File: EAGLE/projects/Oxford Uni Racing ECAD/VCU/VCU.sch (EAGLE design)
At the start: 25 parts, among them J1 PWR_CAN, J2 ASS, J3 MC_LEFT, J4 MC_RIGHT, K1 RT444012, X2 D-SUB9-H2M09ST

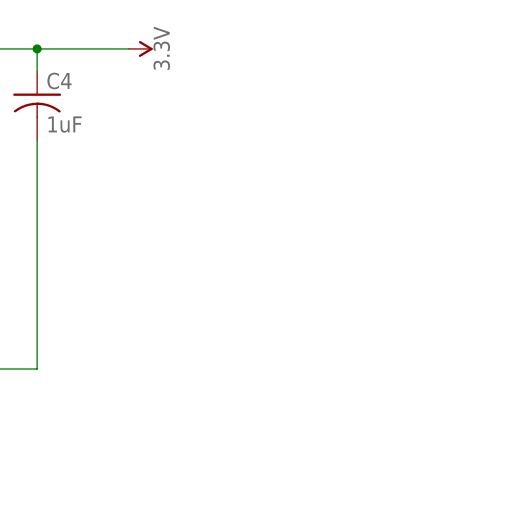
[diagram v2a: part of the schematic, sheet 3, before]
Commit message: added indicator LEDs to boards
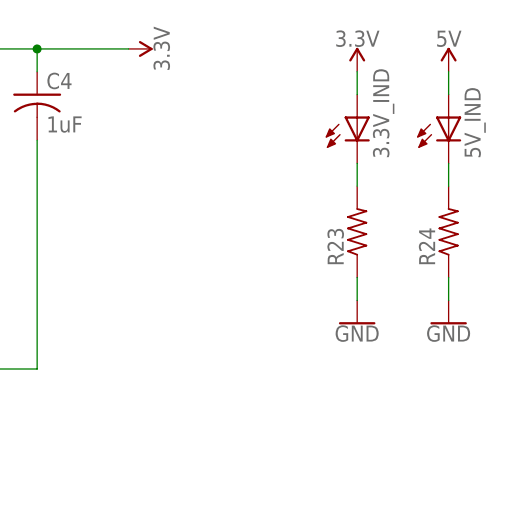
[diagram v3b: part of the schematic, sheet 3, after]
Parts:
- added 3.3V_IND, 5V_IND: (no value), adafruit:LED3MM
- added R23, R24: (no value), adafruit:R-US_0204/7
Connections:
- new net N$12: 3.3V_IND.C, R23.2
- new net N$5: 5V_IND.C, R24.2
- net 3.3V: now also 3.3V_IND.A
- net 5V: now also 5V_IND.A
- net GND: now also R23.1, R24.1
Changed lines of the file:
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@@
 <part name="J2" library="T821108A1S100CEU" deviceset="T821108A1S100CEU" device="" value="ASS"/>
 <part name="F1" library="fuse" library_urn="urn:adsk.eagle:library:233" deviceset="FUSE" device="BLANK_5X20MM" package3d_urn="urn:adsk.eagle:package:14079/1" value="1A"/>
+<part name="3.3V_IND" library="adafruit" library_urn="urn:adsk.eagle:library:420" deviceset="LED" device="3MM" package3d_urn="urn:adsk.eagle:package:6240537/1"/>
+<part name="R23" library="adafruit" library_urn="urn:adsk.eagle:library:420" deviceset="R-US_" device="0204/7" package3d_urn="urn:adsk.eagle:package:6240596/1"/>
+<part name="SUPPLY47" library="SparkFun-PowerSymbols" library_urn="urn:adsk.eagle:library:530" deviceset="3.3V" device=""/>
+<part name="GND30" library="SparkFun-PowerSymbols" library_urn="urn:adsk.eagle:library:530" deviceset="GND" device=""/>
+<part name="5V_IND" library="adafruit" library_urn="urn:adsk.eagle:library:420" deviceset="LED" device="3MM" package3d_urn="urn:adsk.eagle:package:6240537/1"/>
+<part name="R24" library="adafruit" library_urn="urn:adsk.eagle:library:420" deviceset="R-US_" device="0204/7" package3d_urn="urn:adsk.eagle:package:6240596/1"/>
+<part name="SUPPLY54" library="SparkFun-PowerSymbols" library_urn="urn:adsk.eagle:library:530" deviceset="5V" device=""/>
+<part name="GND33" library="SparkFun-PowerSymbols" library_urn="urn:adsk.eagle:library:530" deviceset="GND" device=""/>
 </parts>
 <sheets>
@@
 <attribute name="VALUE" x="114.3" y="9.906" size="1.778" layer="96" align="top-center"/>
 </instance>
+<instance part="3.3V_IND" gate="G$1" x="170.18" y="96.52" smashed="yes">
+<attribute name="NAME" x="173.736" y="91.948" size="1.778" layer="95" rot="R90"/>
+<attribute name="VALUE" x="175.895" y="91.948" size="1.778" layer="96" rot="R90"/>
+</instance>
+<instance part="R23" gate="G$1" x="170.18" y="83.82" smashed="yes" rot="R90">
+<attribute name="NAME" x="168.6814" y="80.01" size="1.778" layer="95" rot="R90"/>
+<attribute name="VALUE" x="173.482" y="80.01" size="1.778" layer="96" rot="R90"/>
+</instance>
+<instance part="SUPPLY47" gate="G$1" x="170.18" y="101.6" smashed="yes">
+<attribute name="VALUE" x="170.18" y="104.394" size="1.778" layer="96" align="bottom-center"/>
+</instance>
+<instance part="GND30" gate="1" x="170.18" y="73.66" smashed="yes">
+<attribute name="VALUE" x="170.18" y="73.406" size="1.778" layer="96" align="top-center"/>
+</instance>
+<instance part="5V_IND" gate="G$1" x="180.34" y="96.52" smashed="yes">
+<attribute name="NAME" x="183.896" y="91.948" size="1.778" layer="95" rot="R90"/>
+<attribute name="VALUE" x="186.055" y="91.948" size="1.778" layer="96" rot="R90"/>
+</instance>
+<instance part="R24" gate="G$1" x="180.34" y="83.82" smashed="yes" rot="R90">
+<attribute name="NAME" x="178.8414" y="80.01" size="1.778" layer="95" rot="R90"/>
+<attribute name="VALUE" x="183.642" y="80.01" size="1.778" layer="96" rot="R90"/>
+</instance>
+<instance part="SUPPLY54" gate="G$1" x="180.34" y="101.6" smashed="yes">
+<attribute name="VALUE" x="180.34" y="104.394" size="1.778" layer="96" align="bottom-center"/>
+</instance>
+<instance part="GND33" gate="1" x="180.34" y="73.66" smashed="yes">
+<attribute name="VALUE" x="180.34" y="73.406" size="1.778" layer="96" align="top-center"/>
+</instance>
 </instances>
 <busses>
@@
 <junction x="124.46" y="48.26"/>
 </segment>
+<segment>
+<pinref part="5V_IND" gate="G$1" pin="A"/>
+<pinref part="SUPPLY54" gate="G$1" pin="5V"/>
+<wire x1="180.34" y1="99.06" x2="180.34" y2="101.6" width="0.1524" layer="91"/>
+</segment>
 </net>
 <net name="3.3V" class="0">
@@
 <pinref part="SUPPLY25" gate="G$1" pin="3.3V"/>
 </segment>
+<segment>
+<pinref part="3.3V_IND" gate="G$1" pin="A"/>
+<pinref part="SUPPLY47" gate="G$1" pin="3.3V"/>
+<wire x1="170.18" y1="99.06" x2="170.18" y2="101.6" width="0.1524" layer="91"/>
+</segment>
 </net>
 <net name="GND" class="0">
@@
 <wire x1="134.62" y1="12.7" x2="114.3" y2="12.7" width="0.1524" layer="91"/>
 </segment>
+<segment>
+<pinref part="R24" gate="G$1" pin="1"/>
+<pinref part="GND33" gate="1" pin="GND"/>
+<wire x1="180.34" y1="78.74" x2="180.34" y2="76.2" width="0.1524" layer="91"/>
+</segment>
+<segment>
+<pinref part="GND30" gate="1" pin="GND"/>
+<pinref part="R23" gate="G$1" pin="1"/>
+<wire x1="170.18" y1="76.2" x2="170.18" y2="78.74" width="0.1524" layer="91"/>
+</segment>
 </net>
 <net name="CANH" class="0">
@@
 </segment>
 </net>
+<net name="N$5" class="0">
+<segment>
+<pinref part="5V_IND" gate="G$1" pin="C"/>
+<pinref part="R24" gate="G$1" pin="2"/>
+<wire x1="180.34" y1="91.44" x2="180.34" y2="88.9" width="0.1524" layer="91"/>
+</segment>
+</net>
+<net name="N$12" class="0">
+<segment>
+<pinref part="R23" gate="G$1" pin="2"/>
+<pinref part="3.3V_IND" gate="G$1" pin="C"/>
+<wire x1="170.18" y1="88.9" x2="170.18" y2="91.44" width="0.1524" layer="91"/>
+</segment>
+</net>

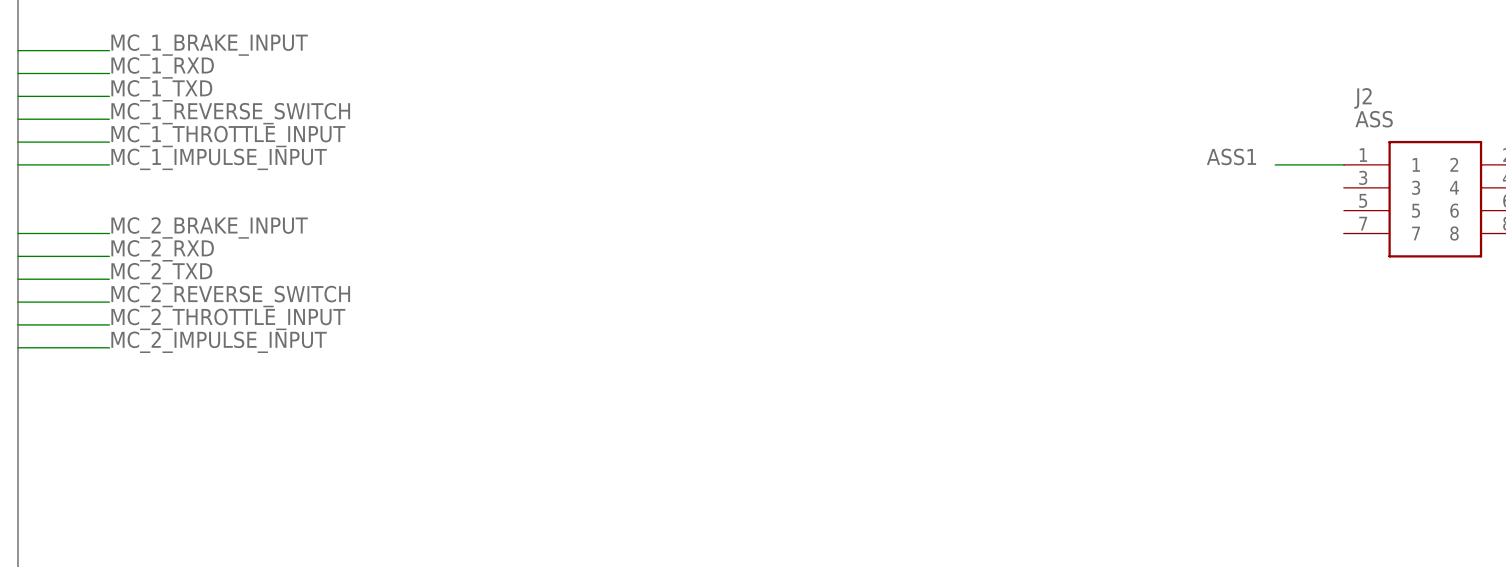
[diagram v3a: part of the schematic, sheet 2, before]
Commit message: added air coil connection on VCU
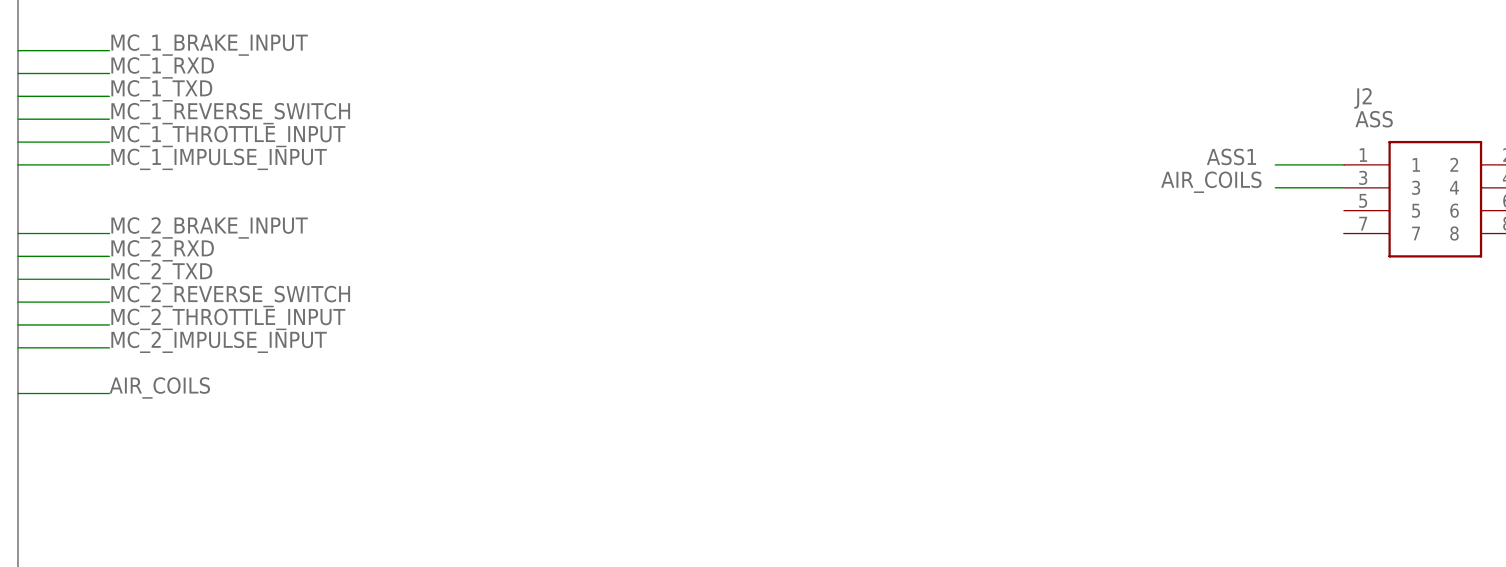
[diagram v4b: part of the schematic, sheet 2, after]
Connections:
- new net AIR_COILS: J2.3, U$1.J5030-D7
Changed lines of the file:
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@@
+</segment>
+</net>
+<net name="AIR_COILS" class="0">
+<segment>
+<wire x1="0" y1="27.94" x2="10.16" y2="27.94" width="0.1524" layer="91"/>
+<label x="10.16" y="27.94" size="1.778" layer="95"/>
 </segment>
 </net>
@@
 </segment>
 </net>
+<net name="AIR_COILS" class="0">
+<segment>
+<wire x1="0" y1="27.94" x2="10.16" y2="27.94" width="0.1524" layer="91"/>
+<label x="10.16" y="27.94" size="1.778" layer="95"/>
+</segment>
+<segment>
+<pinref part="J2" gate="G$1" pin="3"/>
+<wire x1="147.32" y1="50.8" x2="139.7" y2="50.8" width="0.1524" layer="91"/>
+<label x="127" y="50.8" size="1.778" layer="95"/>
+</segment>
+</net>
 </nets>
 </sheet>
@@
 </segment>
 </net>
+<net name="AIR_COILS" class="0">
+<segment>
+<wire x1="0" y1="27.94" x2="10.16" y2="27.94" width="0.1524" layer="91"/>
+<label x="10.16" y="27.94" size="1.778" layer="95"/>
+</segment>
+</net>
 </nets>
 </sheet>
@@
 </instances>
 <busses>
-<bus name="3.3V,5V,12V,ASS1,ASS2,CANH,CANL,GND,MC_1_BRAKE_INPUT,MC_1_IMPULSE_INPUT,MC_1_REVERSE_SWITCH,MC_1_RXD,MC_1_THROTTLE_INPUT,MC_1_TXD,MC_2_BRAKE_INPUT,MC_2_IMPULSE_INPUT,MC_2_REVERSE_SWITCH,MC_2_RXD,MC_2_THROTTLE_INPUT,MC_2_TXD">
+<bus name="3.3V,5V,12V,AIR_COILS,ASS1,ASS2,CANH,CANL,GND,MC_1_BRAKE_INPUT,MC_1_IMPULSE_INPUT,MC_1_REVERSE_SWITCH,MC_1_RXD,MC_1_THROTTLE_INPUT,MC_1_TXD,MC_2_BRAKE_INPUT,MC_2_IMPULSE_INPUT,MC_2_REVERSE_SWITCH,MC_2_RXD,MC_2_THROTTLE_INPUT,MC_2_TXD">
 <segment>
 <wire x1="0" y1="0" x2="0" y2="96.52" width="0.762" layer="92"/>
@@
 <pinref part="BR_LIGHTS_TR" gate="G$1" pin="D"/>
 <wire x1="360.68" y1="132.08" x2="360.68" y2="121.92" width="0.1524" layer="91"/>
+</segment>
+</net>
+<net name="AIR_COILS" class="0">
+<segment>
+<pinref part="U$1" gate="G$1" pin="J5030-D7"/>
+<wire x1="287.02" y1="83.82" x2="304.8" y2="83.82" width="0.1524" layer="91"/>
+<label x="304.8" y="83.82" size="1.778" layer="95"/>
+</segment>
+<segment>
+<wire x1="0" y1="27.94" x2="10.16" y2="27.94" width="0.1524" layer="91"/>
+<label x="10.16" y="27.94" size="1.778" layer="95"/>
 </segment>
 </net>
@@
 </segment>
 </net>
+<net name="AIR_COILS" class="0">
+<segment>
+<wire x1="0" y1="27.94" x2="10.16" y2="27.94" width="0.1524" layer="91"/>
+<label x="10.16" y="27.94" size="1.778" layer="95"/>
+</segment>
+</net>
 </nets>
 </sheet>
@@
 </segment>
 </net>
+<net name="AIR_COILS" class="0">
+<segment>
+<wire x1="0" y1="27.94" x2="10.16" y2="27.94" width="0.1524" layer="91"/>
+<label x="10.16" y="27.94" size="1.778" layer="95"/>
+</segment>
+</net>

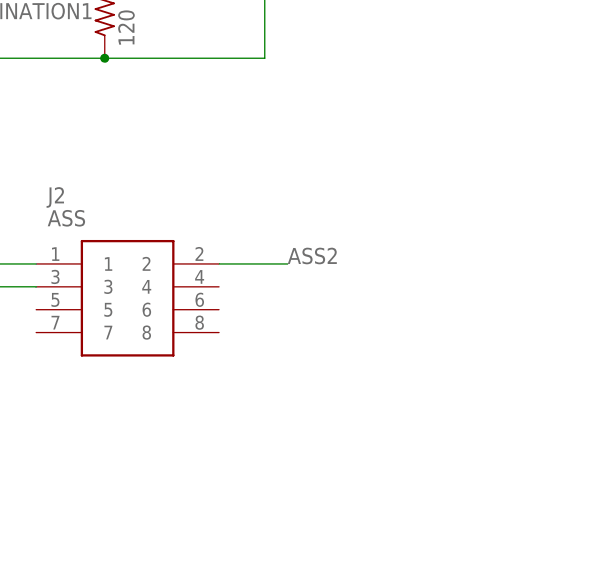
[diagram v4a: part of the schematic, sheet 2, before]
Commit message: added power pin for air coils
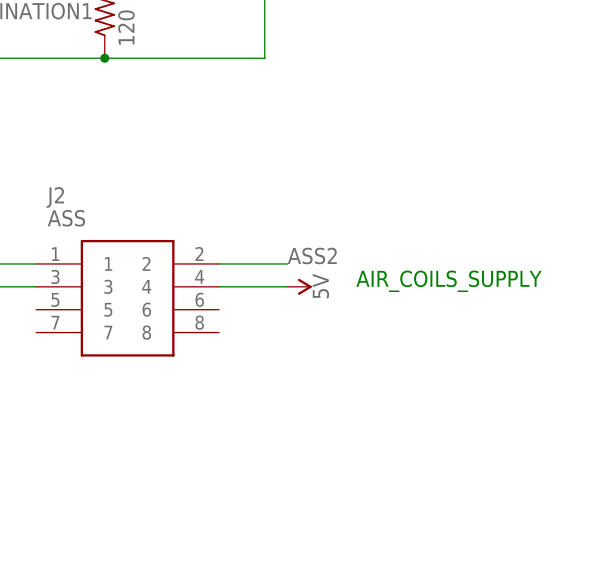
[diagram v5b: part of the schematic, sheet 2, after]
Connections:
- net 5V: now also J2.4
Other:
- note added: "AIR_COILS_SUPPLY"
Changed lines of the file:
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@@
 <part name="SUPPLY54" library="SparkFun-PowerSymbols" library_urn="urn:adsk.eagle:library:530" deviceset="5V" device=""/>
 <part name="GND33" library="SparkFun-PowerSymbols" library_urn="urn:adsk.eagle:library:530" deviceset="GND" device=""/>
+<part name="SUPPLY22" library="SparkFun-PowerSymbols" library_urn="urn:adsk.eagle:library:530" deviceset="5V" device=""/>
 </parts>
 <sheets>
@@
 <plain>
 <text x="0" y="0" size="1.778" layer="91">CROSS_SHEET_CONNECTIONS</text>
+<text x="182.88" y="50.8" size="1.778" layer="91">AIR_COILS_SUPPLY</text>
 </plain>
 <instances>
@@
 <attribute name="VALUE" x="160.401" y="120.65" size="1.778" layer="96" rot="R90"/>
 </instance>
+<instance part="SUPPLY22" gate="G$1" x="175.26" y="50.8" smashed="yes" rot="R270">
+<attribute name="VALUE" x="178.054" y="50.8" size="1.778" layer="96" rot="R270" align="bottom-center"/>
+</instance>
 </instances>
 <busses>
@@
 <wire x1="81.28" y1="78.74" x2="99.06" y2="78.74" width="0.1524" layer="91"/>
 </segment>
-</net>
+<segment>
+<pinref part="J2" gate="G$1" pin="4"/>
+<wire x1="167.64" y1="50.8" x2="175.26" y2="50.8" width="0.1524" layer="91"/>
+<pinref part="SUPPLY22" gate="G$1" pin="5V"/>
+</segment>
+</net>

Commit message: updated VCU with brake lights
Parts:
- added BR_LIGHTS_TR1: IRLML2502GTRPBF, adafruit:MOSFET-NREFLOW
- added F2: 1.5A, fuse:FUSEBLANK_5X20MM
- added R12: 1K, adafruit:R-US_0204/7
- added R13: 47K, adafruit:R-US_0204/7
- J2: value ASS -> ASS+BRAKE_LIGHTS
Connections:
- new net BRAKE_LIGHTS+: F2.2, J2.5
- new net BRAKE_LIGHTS-: BR_LIGHTS_TR1.D, J2.6
- new net BRAKE_LIGHTS_OUT: R12.1, U$1.J5009-D8
- new net N$25: BR_LIGHTS_TR1.G, R12.2, R13.2
- net 12V_BATTERY: now also F2.1
- net GND: now also BR_LIGHTS_TR1.S, R13.1

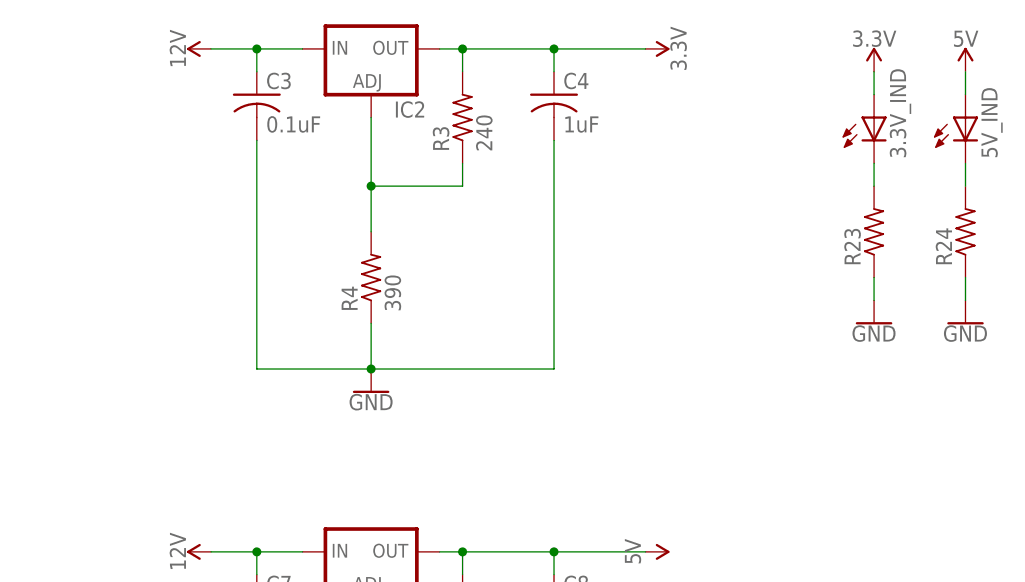
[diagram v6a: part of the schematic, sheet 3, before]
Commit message: removed 3.3V regulators from boards, as we will be using the onbloard regulator
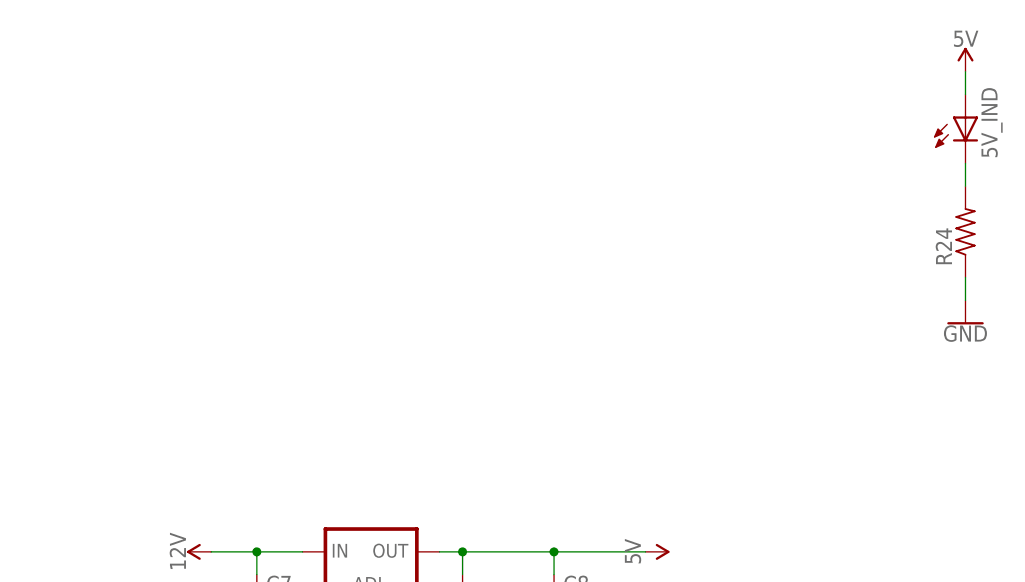
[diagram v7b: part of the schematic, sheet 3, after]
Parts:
- removed 3.3V_IND: (no value), adafruit:LED3MM
- removed C3: 0.1uF, adafruit:C-US050-025X075
- removed C4: 1uF, adafruit:C-US050-025X075
- removed IC2: (no value), v-reg:LM317TS
- removed R23: (no value), adafruit:R-US_0204/7
- removed R3: 240, adafruit:R-US_0204/7
- removed R4: 390, adafruit:R-US_0204/7
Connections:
- removed net N$12: 3.3V_IND.C, R23.2
- removed net N$2: IC2.ADJ, R3.1, R4.2
- net 12V: no longer C3.1, IC2.IN
- net 3.3V: now also U$1.J5013-3V3; no longer 3.3V_IND.A, C4.1, IC2.OUT, R3.2
- net 5V: now also U$1.J5014-5V0
- net GND: now also U$1.J5015-GND, U$1.J5016-GND; no longer C3.2, C4.2, R23.1, R4.1
